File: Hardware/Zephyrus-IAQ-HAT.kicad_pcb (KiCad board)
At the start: 2 copper layers, 65 x 56 mm, 85 parts, among them J1 Conn_02x20_Odd_Even__Rpi, J10 A1, J11 A2, J12 A3, J13 A4, J14 A5, J15 Alert, J16 Conn_01x02_Male, J16 I2C 5V, J17 PPS, J2 USART, J3 Jumper, J4 Fan 1, J5 Fan 2, J6 I2C 3.3V, J7 10103594-0001LF, J8 I2C 3.3V, J9 A0, U1 EEPROM, U10 5V, U11 Vshift, U2 FAN, U3 BUF, U4 BSS138, U5 BSS138, U6 BUF, U7 DAC, U8 MUX, U9 ADC

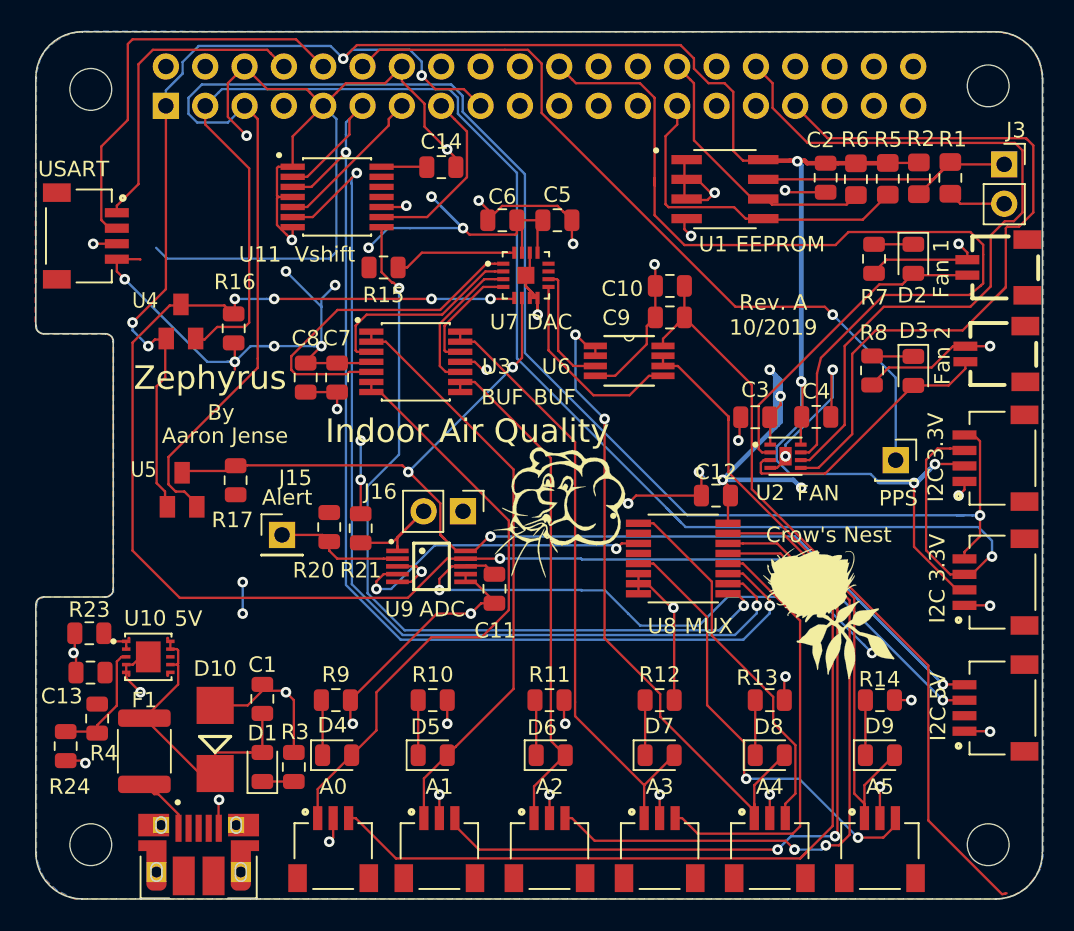
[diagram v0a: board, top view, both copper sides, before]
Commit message: Organized schematic naming
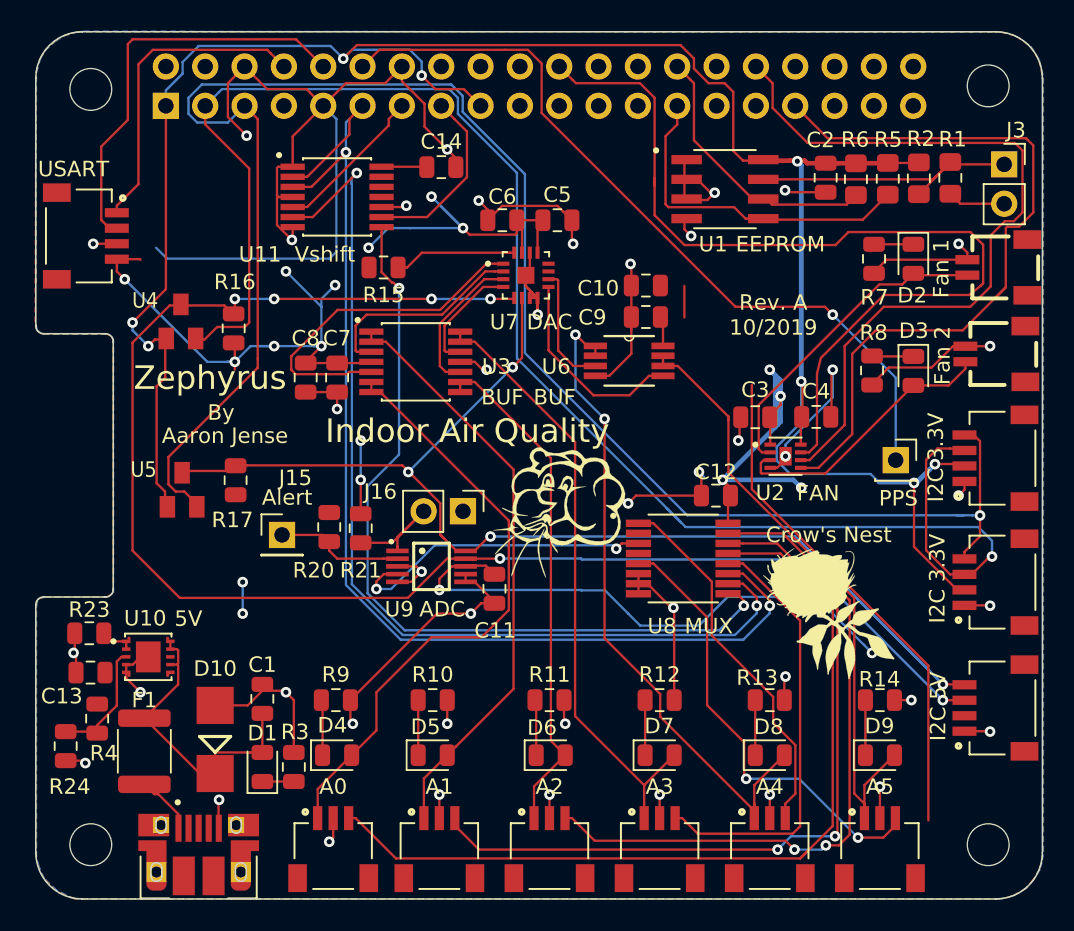
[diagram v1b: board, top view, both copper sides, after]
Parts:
- moved C9 1.55 mm to (239.4, 112.4)
- moved C10 1.55 mm to (239.4, 110.4)
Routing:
- net +5V: track 186.4 -> 172.0 mm
- net GND: track 215.9 -> 215.0 mm
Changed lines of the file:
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@@
     (thickness 1.6)
     (drawings 52)
-    (tracks 991)
+    (tracks 985)
     (zones 0)
     (modules 85)
@@
   )
   (layers
-    (0 F.Cu signal)
-    (31 B.Cu signal)
-    (32 B.Adhes user)
+    (0 F.Cu signal hide)
+    (31 B.Cu signal hide)
+    (32 B.Adhes user hide)
     (33 F.Adhes user)
     (34 B.Paste user)
@@
     (37 F.SilkS user)
     (38 B.Mask user)
-    (39 F.Mask user hide)
+    (39 F.Mask user)
     (40 Dwgs.User user)
     (41 Cmts.User user)
@@
   )
   (module Capacitor_SMD:C_0805_2012Metric (layer F.Cu)
-    (at 240.9444 110.4138 180)
+    (at 239.395 110.3884 180)
     (descr "Capacitor SMD 0805 (2012 Metric), square (rectangular) end terminal, IPC_7351 nominal, (Body size source: https://docs.google.com/spreadsheets/d/1BsfQQcO9C6DZCsRaXUlFlo91Tg2WpOkGARC1WS5S8t0/edit?usp=sharing), generated with kicad-footprint-generator")
     (tags capacitor)
@@
   )
   (module Capacitor_SMD:C_0805_2012Metric (layer F.Cu)
-    (at 240.9444 112.4458 180)
+    (at 239.395 112.4204 180)
     (descr "Capacitor SMD 0805 (2012 Metric), square (rectangular) end terminal, IPC_7351 nominal, (Body size source: https://docs.google.com/spreadsheets/d/1BsfQQcO9C6DZCsRaXUlFlo91Tg2WpOkGARC1WS5S8t0/edit?usp=sharing), generated with kicad-footprint-generator")
     (tags capacitor)
@@
   (segment (start 244.698 124.11) (end 244.856 123.952) (width 0.1524) (layer F.Cu) (net 1))
   (segment (start 244.698 125.741) (end 244.698 124.11) (width 0.1524) (layer F.Cu) (net 1))
-  (segment (start 241.3874 112.9403) (end 241.8819 112.4458) (width 0.1524) (layer F.Cu) (net 1))
   (segment (start 241.8819 112.4458) (end 241.8819 110.4138) (width 0.1524) (layer F.Cu) (net 1))
   (segment (start 231.398 106.5085) (end 231.0615 106.172) (width 0.1524) (layer F.Cu) (net 1))
@@
   (segment (start 247.427 118.9205) (end 247.396 118.8895) (width 0.1524) (layer F.Cu) (net 1))
   (segment (start 247.427 120.662) (end 247.427 118.9205) (width 0.1524) (layer F.Cu) (net 1))
-  (segment (start 262.591679 149.656243) (end 262.688307 149.632859) (width 0.1524) (layer F.Cu) (net 1))
-  (segment (start 262.494294 149.676077) (end 262.591679 149.656243) (width 0.1524) (layer F.Cu) (net 1))
   (segment (start 246.23711 116.80101) (end 246.23711 123.534026) (width 0.1524) (layer F.Cu) (net 1))
-  (segment (start 241.8819 112.4458) (end 246.23711 116.80101) (width 0.1524) (layer F.Cu) (net 1))
   (segment (start 246.23711 123.534026) (end 257.636601 134.933517) (width 0.1524) (layer F.Cu) (net 1))
   (segment (start 257.636601 134.933517) (end 257.636601 144.932726) (width 0.1524) (layer F.Cu) (net 1))
-  (segment (start 257.636601 144.932726) (end 262.39622 149.692345) (width 0.1524) (layer F.Cu) (net 1))
-  (segment (start 262.39622 149.692345) (end 262.494294 149.676077) (width 0.1524) (layer F.Cu) (net 1))
-  (segment (start 240.4999 113.8278) (end 241.8819 112.4458) (width 0.1524) (layer F.Cu) (net 1))
-  (segment (start 240.4999 114.2873) (end 240.4999 113.8278) (width 0.1524) (layer F.Cu) (net 1))
   (via (at 254 134.112) (size 0.6858) (drill 0.3302) (layers F.Cu B.Cu) (net 1))
   (via (at 226.06 130.048) (size 0.6858) (drill 0.3302) (layers F.Cu B.Cu) (net 1))
@@
   (segment (start 235.230706 130.074706) (end 235.230706 130.048) (width 0.1524) (layer B.Cu) (net 1))
   (segment (start 226.8646 128.524) (end 226.06 129.3286) (width 0.1524) (layer F.Cu) (net 1))
+  (segment (start 240.4999 112.5878) (end 240.3325 112.4204) (width 0.1524) (layer F.Cu) (net 1))
+  (segment (start 240.4999 114.2873) (end 240.4999 112.5878) (width 0.1524) (layer F.Cu) (net 1))
   (segment (start 217.424 117.2695) (end 219.456 117.2695) (width 0.1524) (layer F.Cu) (net 2))
   (segment (start 227.752 129.024) (end 227.752 129.524) (width 0.1524) (layer F.Cu) (net 2))
@@
   (segment (start 228.337 129.524) (end 229.616 130.803) (width 0.1524) (layer F.Cu) (net 2))
   (segment (start 227.752 129.524) (end 228.337 129.524) (width 0.1524) (layer F.Cu) (net 2))
-  (segment (start 240.0069 112.4458) (end 240.0069 110.4138) (width 0.1524) (layer F.Cu) (net 2))
+  (segment (start 238.4575 112.4204) (end 238.4575 110.3884) (width 0.1524) (layer F.Cu) (net 2))
   (segment (start 253.492 116.7615) (end 254 116.7615) (width 0.1524) (layer F.Cu) (net 2))
   (segment (start 259.2256 114.308) (end 260.153 114.308) (width 0.1524) (layer F.Cu) (net 2))
@@
   (via (at 248.412 121.412) (size 0.6858) (drill 0.3302) (layers F.Cu B.Cu) (net 2))
   (segment (start 238.918 129.641) (end 238.918 130.291) (width 0.1524) (layer F.Cu) (net 2))
-  (via (at 239.9538 109.0168) (size 0.6858) (drill 0.3302) (layers F.Cu B.Cu) (net 2))
+  (via (at 238.4044 108.9914) (size 0.6858) (drill 0.3302) (layers F.Cu B.Cu) (net 2))
   (via (at 254.508 142.748) (size 0.6858) (drill 0.3302) (layers F.Cu B.Cu) (net 2))
   (segment (start 254.508 144.78) (end 254.508 142.748) (width 0.1524) (layer F.Cu) (net 2))
@@
   (segment (start 239.493 129.641) (end 241.043 131.191) (width 0.1524) (layer F.Cu) (net 2))
   (segment (start 238.918 129.641) (end 239.493 129.641) (width 0.1524) (layer F.Cu) (net 2))
-  (segment (start 240.0069 109.0699) (end 239.9538 109.0168) (width 0.1524) (layer F.Cu) (net 2))
-  (segment (start 240.0069 110.4138) (end 240.0069 109.0699) (width 0.1524) (layer F.Cu) (net 2))
-  (segment (start 239.450663 113.002037) (end 240.0069 112.4458) (width 0.1524) (layer F.Cu) (net 2))
-  (segment (start 239.450663 114.175759) (end 239.450663 113.002037) (width 0.1524) (layer F.Cu) (net 2))
-  (segment (start 237.408722 116.2177) (end 239.450663 114.175759) (width 0.1524) (layer F.Cu) (net 2))
-  (segment (start 236.1311 116.2177) (end 237.408722 116.2177) (width 0.1524) (layer F.Cu) (net 2))
+  (segment (start 238.4575 109.0445) (end 238.4044 108.9914) (width 0.1524) (layer F.Cu) (net 2))
+  (segment (start 238.4575 110.3884) (end 238.4575 109.0445) (width 0.1524) (layer F.Cu) (net 2))
+  (segment (start 238.4575 113.2204) (end 238.4575 112.4204) (width 0.1524) (layer F.Cu) (net 2))
+  (segment (start 238.4575 114.793) (end 238.4575 113.2204) (width 0.1524) (layer F.Cu) (net 2))
+  (segment (start 237.0328 116.2177) (end 238.4575 114.793) (width 0.1524) (layer F.Cu) (net 2))
+  (segment (start 236.1311 116.2177) (end 237.0328 116.2177) (width 0.1524) (layer F.Cu) (net 2))
   (segment (start 208.3585 124.5565) (end 208.346 124.544) (width 0.1524) (layer F.Cu) (net 3))
   (segment (start 208.3585 113.8885) (end 208.346 113.876) (width 0.1524) (layer F.Cu) (net 3))
@@
   (segment (start 244.72639 122.454372) (end 252.85439 130.582372) (width 0.1524) (layer F.Cu) (net 42))
   (segment (start 240.4999 114.9223) (end 240.4999 115.5827) (width 0.1524) (layer F.Cu) (net 42))
-  (segment (start 244.72639 118.850588) (end 244.72639 119.07781) (width 0.1524) (layer F.Cu) (net 42))
-  (segment (start 241.458502 115.5827) (end 244.72639 118.850588) (width 0.1524) (layer F.Cu) (net 42))
   (segment (start 240.4999 115.5827) (end 241.458502 115.5827) (width 0.1524) (layer F.Cu) (net 42))
+  (segment (start 241.458502 115.5827) (end 244.72639 118.850588) (width 0.1524) (layer F.Cu) (net 42))
   (segment (start 244.72639 118.81299) (end 244.72639 119.07781) (width 0.1524) (layer F.Cu) (net 42))
+  (segment (start 244.72639 118.850588) (end 244.72639 119.07781) (width 0.1524) (layer F.Cu) (net 42))
   (segment (start 244.72639 119.07781) (end 244.72639 122.454372) (width 0.1524) (layer F.Cu) (net 42))
   (segment (start 253.5705 140.716) (end 253.5705 137.16) (width 0.1524) (layer F.Cu) (net 43))

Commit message: Update PCB to latest schematic changes.
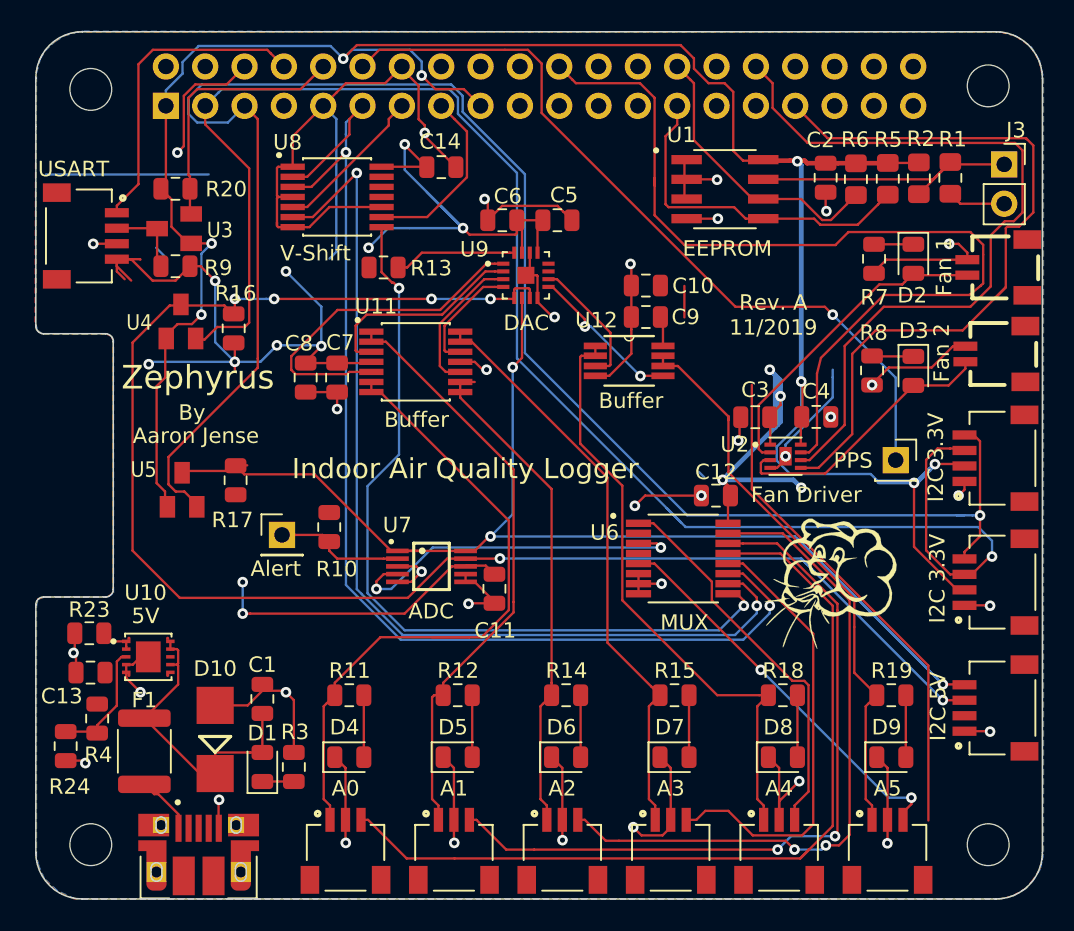
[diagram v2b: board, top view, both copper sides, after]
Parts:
- removed the G*** at (251.2, 131.6)
- removed the J10 at (226.1, 144.8)
- removed the J16 at (227.6, 125.0)
- removed the R10 at (225.6, 137.2)
- removed the R11 at (233.2, 137.2)
- removed the R13 at (247.4, 137.2)
- removed R21: 10K, Resistor_SMD:R_0805_2012Metric
- removed the U8 at (241.8, 128.0)
- added J15: A5, zephyrus-iaq:JST_SM03B-SRSS-TB(LF)(SN), F.Cu at (255.0, 144.9)
- added R15: 330, Resistor_SMD:R_0805_2012Metric, F.Cu at (241.2, 136.8)
- added R18: 330, Resistor_SMD:R_0805_2012Metric, F.Cu at (248.2, 136.8)
- added R19: 330, Resistor_SMD:R_0805_2012Metric, F.Cu at (255.2, 136.8)
- added R20: 10k, Resistor_SMD:R_0805_2012Metric, F.Cu at (209.0, 104.1)
- added R9: 10k, Resistor_SMD:R_0805_2012Metric, F.Cu at (209.0, 109.1)
- added U3: BSS138, zephyrus-iaq:BSS138, F.Cu at (208.9, 106.7)
- added U6: MUX, zephyrus-iaq:SOP65P640X120-16N, F.Cu at (241.8, 128.0)
- J11: value A2 -> A1
- J12: value A3 -> A2
- J13: value A4 -> A3
- J14: value A5 -> A4
- R16, R17: value 3.3k -> 10k
- U11: renamed from U3; value BUF -> Buffer
- U12: renamed from U6; value BUF -> Buffer
- U2: value FAN -> Fan Driver
- U8: renamed from U11; value Vshift -> V-Shift
- moved R14 20.3 mm to (234.2, 136.8), turned to 180 degrees
- moved G*** 18.1 mm to (251.2, 129.6)
- moved R12 13.0 mm to (227.2, 136.8), turned to 180 degrees
- moved J14 6.51 mm to (248.0, 144.9)
- moved J13 6.40 mm to (241.0, 144.9)
- moved J12 6.28 mm to (234.0, 144.9)
- moved J11 6.17 mm to (227.0, 144.9)
- moved D5 1.62 mm to (227.2, 140.8)
- moved D6 1.00 mm to (234.2, 140.8)
- moved D7 0.97 mm to (241.2, 140.8)
- moved R11 0.92 mm to (220.2, 136.8), turned to 180 degrees
- moved D8 0.86 mm to (248.2, 140.8)
- moved J10 0.81 mm to (220.0, 144.9)
- moved D4 0.80 mm to (220.2, 140.8)
- moved D9 0.75 mm to (255.2, 140.8)
- renumbered J9 to J10, J15 to J9, R20 to R10, R9 to R11, R15 to R13, U9 to U7, U7 to U9
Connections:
- net /ADC_Subsystem/ADC_ALERT renamed Net-(J9-Pad1)
- net /Analog_Sensors/DAC_CLR renamed Net-(R13-Pad2)
- net /Analog_Sensors/DAC_OUT_A renamed /Analog Port Control/DAC_OUT_A
- net /Analog_Sensors/DAC_OUT_B renamed /Analog Port Control/DAC_OUT_B
- net /Analog_Sensors/DAC_OUT_C renamed /Analog Port Control/DAC_OUT_C
- net /Analog_Sensors/DAC_OUT_D renamed /Analog Port Control/DAC_OUT_D
- net /Analog_Sensors/DAC_OUT_E renamed /Analog Port Control/DAC_OUT_E
- net /Analog_Sensors/DAC_OUT_F renamed /Analog Port Control/DAC_OUT_F
- net /Fan_Control/FAN_OUT1 renamed Net-(D2-Pad2)
- net /Fan_Control/FAN_OUT2 renamed Net-(D3-Pad2)
- net /PowerManagement/VREG_IN_5V renamed Net-(C1-Pad1)
- net /PowerManagement/VREG_SENSE renamed /Power Management/VREG_SENSE
- D4 pad 1: Net-(D4-Pad1) -> GND
- D4 pad 2: /Analog_Sensors/BUF_OUT_0 -> Net-(D4-Pad2)
- D5 pad 1: Net-(D5-Pad1) -> GND
- D5 pad 2: /Analog_Sensors/BUF_OUT_1 -> Net-(D5-Pad2)
- D6 pad 1: Net-(D6-Pad1) -> GND
- D6 pad 2: /Analog_Sensors/BUF_OUT_2 -> Net-(D6-Pad2)
- D7 pad 1: Net-(D7-Pad1) -> GND
- D7 pad 2: /Analog_Sensors/BUF_OUT_3 -> Net-(D7-Pad2)
- D8 pad 1: Net-(D8-Pad1) -> GND
- D8 pad 2: /Analog_Sensors/BUF_OUT_4 -> Net-(D8-Pad2)
- D9 pad 1: Net-(D9-Pad1) -> GND
- D9 pad 2: /Analog_Sensors/BUF_OUT_5 -> Net-(D9-Pad2)
- J10 pad 1: /Analog_Sensors/BUF_OUT_0 -> /Analog Port Control/BUF_OUT_0
- J11 pad 1: /Analog_Sensors/BUF_OUT_2 -> /Analog Port Control/BUF_OUT_1
- J11 pad 3: /ADC2 -> /ADC1
- J12 pad 1: /Analog_Sensors/BUF_OUT_3 -> /Analog Port Control/BUF_OUT_2
- J12 pad 3: /ADC3 -> /ADC2
- J13 pad 1: /Analog_Sensors/BUF_OUT_4 -> /Analog Port Control/BUF_OUT_3
- J13 pad 3: /ADC4 -> /ADC3
- J14 pad 1: /Analog_Sensors/BUF_OUT_5 -> /Analog Port Control/BUF_OUT_4
- J14 pad 3: /ADC5 -> /ADC4
- J2 pad 2: /GPIO15(RXD0) -> /RXD0
- R11 pad 1: Net-(D4-Pad1) -> Net-(D4-Pad2)
- R11 pad 2: GND -> /Analog Port Control/BUF_OUT_0
- R12 pad 1: Net-(D7-Pad1) -> Net-(D5-Pad2)
- R12 pad 2: GND -> /Analog Port Control/BUF_OUT_1
- R14 pad 1: Net-(D9-Pad1) -> Net-(D6-Pad2)
- R14 pad 2: GND -> /Analog Port Control/BUF_OUT_2
- U11 pad 1: /Analog_Sensors/BUF_OUT_1 -> /Analog Port Control/BUF_OUT_1
- U11 pad 13: /Analog_Sensors/BUF_OUT_3 -> /Analog Port Control/BUF_OUT_3
- U11 pad 14: /Analog_Sensors/BUF_OUT_3 -> /Analog Port Control/BUF_OUT_3
- U11 pad 2: /Analog_Sensors/BUF_OUT_1 -> /Analog Port Control/BUF_OUT_1
- U11 pad 6: /Analog_Sensors/BUF_OUT_0 -> /Analog Port Control/BUF_OUT_0
- U11 pad 7: /Analog_Sensors/BUF_OUT_0 -> /Analog Port Control/BUF_OUT_0
- U11 pad 8: /Analog_Sensors/BUF_OUT_2 -> /Analog Port Control/BUF_OUT_2
- U11 pad 9: /Analog_Sensors/BUF_OUT_2 -> /Analog Port Control/BUF_OUT_2
- U12 pad 1: /Analog_Sensors/BUF_OUT_4 -> /Analog Port Control/BUF_OUT_4
- U12 pad 2: /Analog_Sensors/BUF_OUT_4 -> /Analog Port Control/BUF_OUT_4
- U12 pad 6: /Analog_Sensors/BUF_OUT_5 -> /Analog Port Control/BUF_OUT_5
- U12 pad 7: /Analog_Sensors/BUF_OUT_5 -> /Analog Port Control/BUF_OUT_5
- U7 pad 1: /ADC_Subsystem/ADC_ADDR -> /SCL_5
- U7 pad 4: /ADC_Subsystem/MUL_COM -> Net-(U6-Pad3)
- U8 pad 3: /ADC_Subsystem/MUL_A_5V -> /Multiplexed ADC/MUL_A_5V
- U8 pad 6: /ADC_Subsystem/MUL_B_5V -> /Multiplexed ADC/MUL_B_5V
- U8 pad 8: /ADC_Subsystem/MUL_C_5V -> /Multiplexed ADC/MUL_C_5V
- U9 pad 7: GND -> /SDA_5
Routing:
- net /Multiplexed ADC/MUL_A_5V: track 0.00 -> 68.3 mm, vias 0 -> 2
- net /ADC_Subsystem/MUL_A_5V: track 68.3 -> 0.00 mm, vias 2 -> 0
- net /ADC_Subsystem/MUL_B_5V: track 63.4 -> 0.00 mm, vias 2 -> 0
- net /Multiplexed ADC/MUL_B_5V: track 0.00 -> 63.1 mm, vias 0 -> 2
- net /Multiplexed ADC/MUL_C_5V: track 0.00 -> 52.5 mm, vias 0 -> 2
- net /ADC_Subsystem/MUL_C_5V: track 52.5 -> 0.00 mm, vias 2 -> 0
- net /Analog_Sensors/BUF_OUT_4: track 44.0 -> 0.00 mm, vias 2 -> 0
- net /Analog Port Control/BUF_OUT_0: track 0.00 -> 43.7 mm
- net /Analog_Sensors/BUF_OUT_5: track 40.9 -> 0.00 mm
- net /Analog_Sensors/BUF_OUT_3: track 39.6 -> 0.00 mm
- net /Analog Port Control/BUF_OUT_4: track 0.00 -> 39.5 mm
- net /Analog_Sensors/BUF_OUT_0: track 39.2 -> 0.00 mm
- net /Analog Port Control/BUF_OUT_1: track 0.00 -> 38.6 mm
- net /Analog_Sensors/BUF_OUT_1: track 38.2 -> 0.00 mm
- net /Analog Port Control/BUF_OUT_3: track 0.00 -> 37.8 mm
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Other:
- board text added: "Rev. A 11/2019"
- board text removed: "Indoor Air Quality"
- board text removed: "RASPBERRY-PI 40-PIN ADDON BOARD VIEW FROM TOP NOTE: P1 SHOULD BE FITTED ON THE REVERSE OF THE BOARD ADD EDGE CUTS FROM CAMERA AND DISPLAY PORTS AS REQUIRED"
- board text removed: "Rev. A 10/2019"
